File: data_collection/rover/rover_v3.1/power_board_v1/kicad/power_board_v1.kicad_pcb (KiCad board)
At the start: 4 copper layers, 100 x 65 mm, 136 parts, among them J1 XT60_BATT, J10 from Pi USB2, J11 UPDI prog (UPDI/3V3/GND), J12 5V_A pigtail (DNP), J13 USB_A port3 (3A), J14 from Pi USB3, J2 PANEL_SW, J3 USB4105-GF-A (TH shell), J4 USB_A radio1, J5 USB_A radio2, J6 AUX 5V 2A, J7 PI GPIO harness, J8 AUX_CTL out (JST-GH), J9 from Pi USB1, Q2 CSD18543Q3A diode, Q3 CSD18543Q3A switch, U1 LM5145 rail A, U10 TPS2557 ~3A (always on), U2 LM5145 rail B, U3 ATtiny816-SSN (SOIC-20), U4 LM74800-Q1, U5 INA226 (addr 0x40), U6 TPS7A1633 3V3 60V LDO, U7 TPS2557 ~3A, U8 TPS2557 ~3A, U9 AP2112K-3.3 (switched)

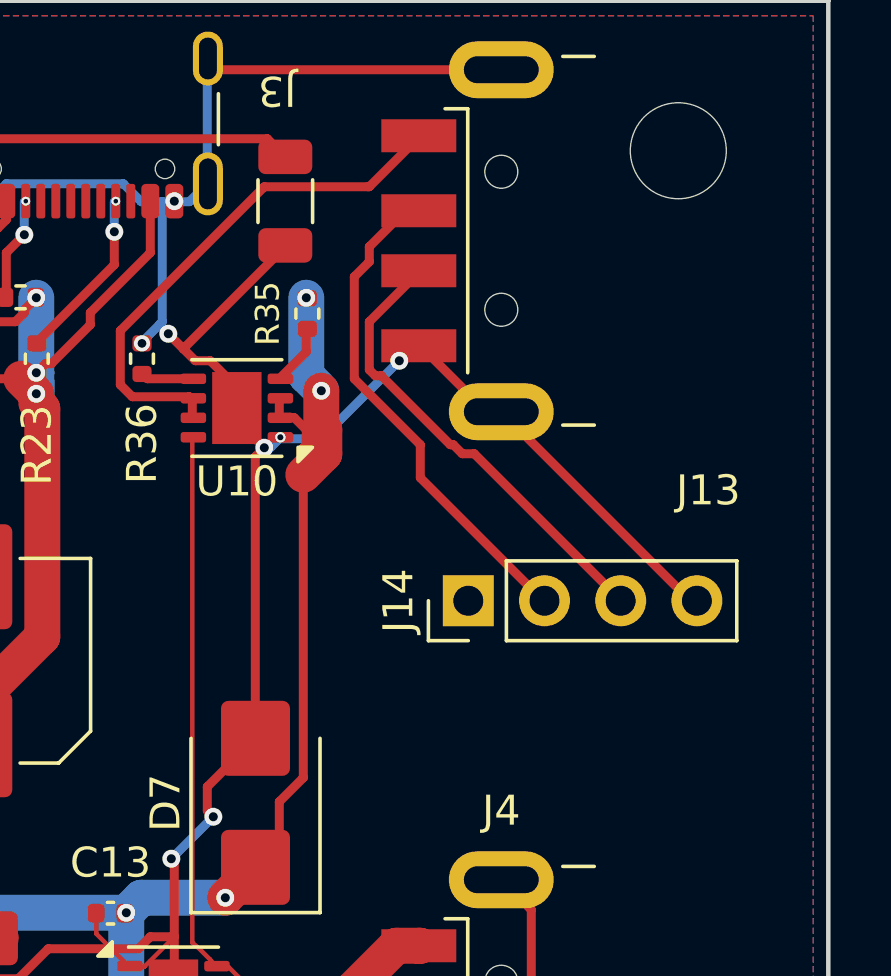
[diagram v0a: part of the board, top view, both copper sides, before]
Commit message: power_board v4.5: add D8 (USB port 3 ESD array) — caught by KiCad 10 schematic-parity
KiCad 10.0.4 re-validation found D8 (USBLC6-2SC6, port 3 ESD) in the
schematic/netlist but absent from the board since v4: the 3-port change
added D8's place() call but not its REF_FP footprint entry, and
generate_board.py silently skipped footprint-less parts. Port 3 data
lines (J14->J13) carried no ESD protection while ports 1/2 had D2/D3.

- board: D8 placed at (138.25,74.16) south of J14; all 6 pads routed
  with exact-collide verification (data stubs F.Cu, VBUS3 via B.Cu lane,
  GND stub+via + pours); one redundant B.Cu GND stitch ripped (pour+plane
  carry GND; DRC 0 unconnected proves it). DRC: 0 violations, 0
  unconnected (severity-all, refill). Audit: PASS (same 3 known warns).
- generators: D8 added to REF_FP; missing footprint is now a HARD ERROR;
  netlist parser whitespace-tolerant (KiCad 10 pretty-prints netlists)
  with parsed-0 guards
- netlist.net regenerated (D8 complete + stale pre-SOIC U3 numbering)
- audit_board.py: KiCad >=9 compat (EDA_UNITS rename; WriteDRCReport
  segfaults headless -> kicad-cli drc fallback)
- fab/: full re-export on KiCad 10 (In1/In2 now .g1/.g2 - v10 protel
  naming; stale v7 gerbers + unused User_* layers removed), BOM line
  USBLC6-2SC6 now D2,D3,D8; upload zip added
- .kicad_pro: KiCad 10 format migration (float cleanup + new keys only;
  all rule floors and severities preserved, .kicad_dru untouched)
- .claude/settings.json: read-only tool allowlist (kicad-cli exports,
  pdftoppm/pdfinfo, rsvg-convert, nvidia-smi queries)
- docs/learnings.md: the silent-skip lesson + parity gate rule

Co-Authored-By: Claude Fable 5 <noreply@anthropic.com>
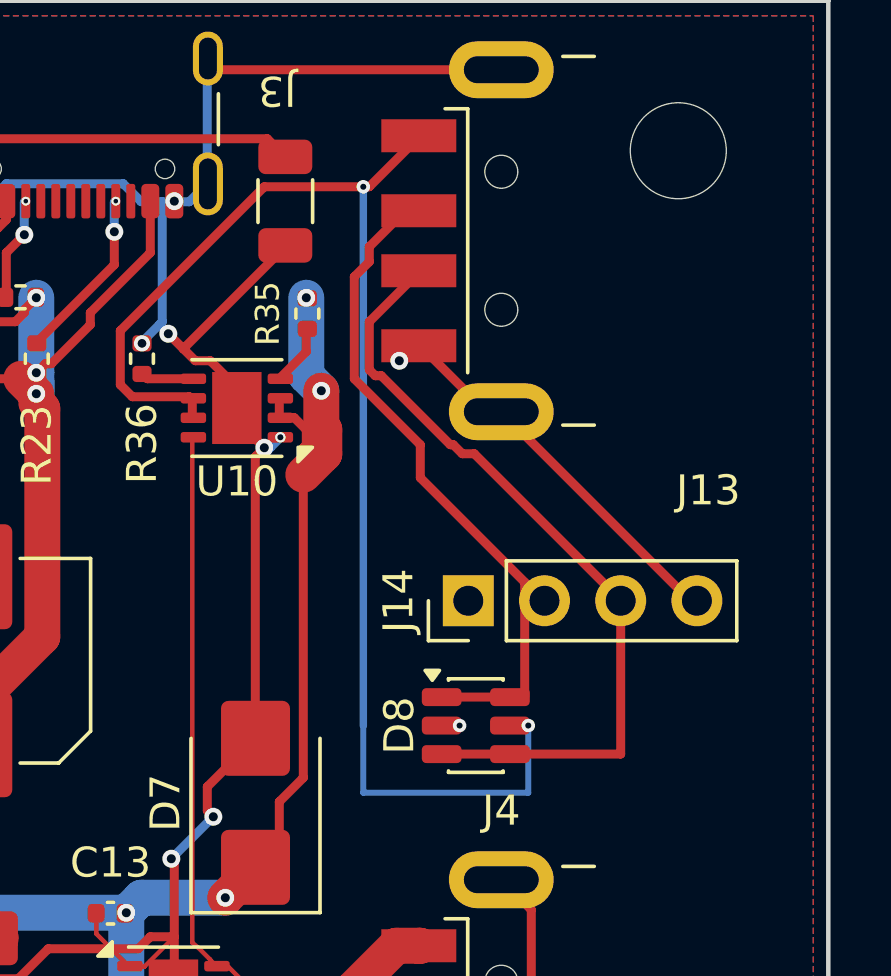
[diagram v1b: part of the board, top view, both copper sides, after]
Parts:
- added D8: USBLC6-2SC6, SOT-23-6, F.Cu at (138.2, 74.2)
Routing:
- net VBUS3: track 17.8 -> 46.4 mm, vias 0 -> 2
- net D3_P: track 15.6 -> 26.7 mm
- net D3_N: track 16.9 -> 23.5 mm
- net GND: track 748.0 -> 743.5 mm, vias 98 -> 99

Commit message: power_board v4.5: sync U3 value to ATtiny1616-SN across generator/sch/netlist/board/BOM/CPL
Closes the drift from the LCSC-only substitution (33571a4): U3's value now
reads 'ATtiny1616-SN (816-compat)' everywhere — schematic PDF, assembly
docs, and BOM Comment agree with the part JLC actually places (C614136).
Also retires the never-orderable 'ATtiny816-SSN' string. DRC/parity
re-verified: 0/0/0. Submission zip rebuilt.

Co-Authored-By: Claude Fable 5 <noreply@anthropic.com>
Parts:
- U3: value ATtiny816-SSN (SOIC-20) -> ATtiny1616-SN (816-compat)
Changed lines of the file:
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@@
 			)
 		)
-		(property "Value" "ATtiny816-SSN (SOIC-20)"
+		(property "Value" "ATtiny1616-SN (816-compat)"
 			(at 0 7.35 0)
 			(layer "F.Fab")

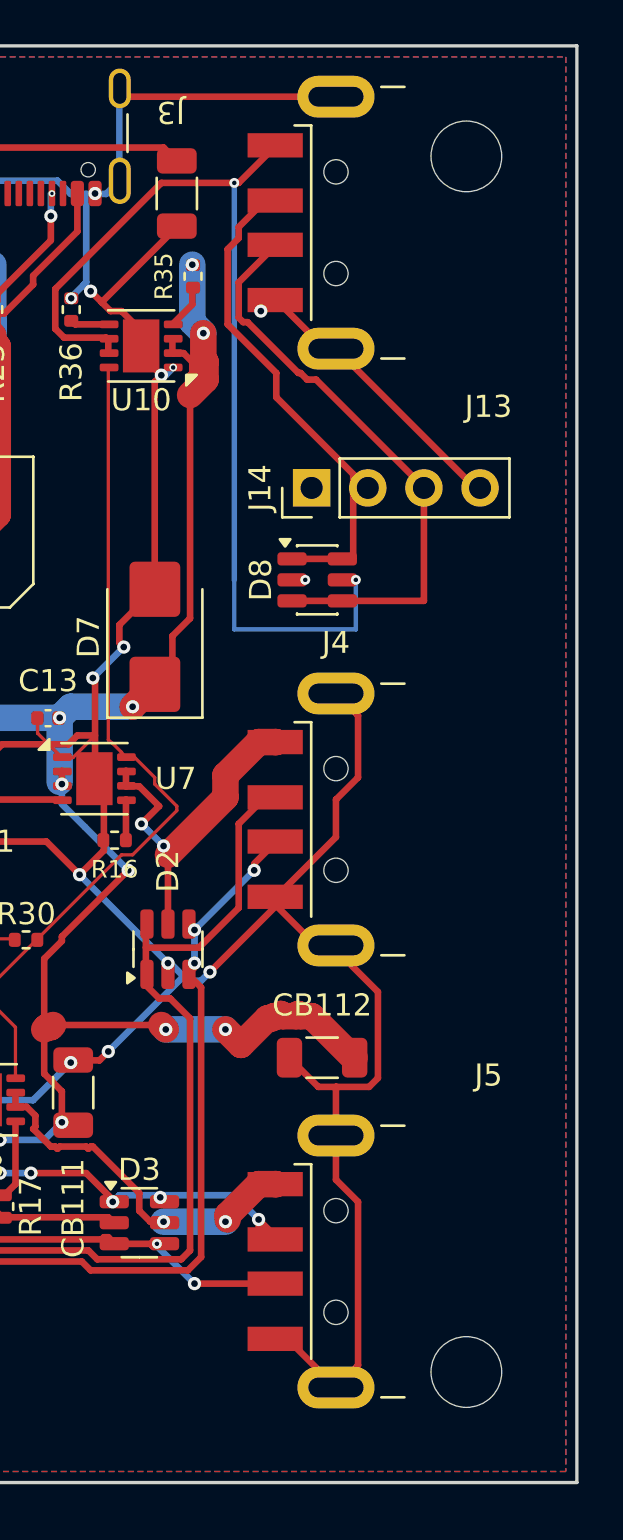
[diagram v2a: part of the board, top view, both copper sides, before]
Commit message: power_board v4.6: relocate H2/H4 mounting holes out from under the USB-A shells
H2 (145,55) and H4 (145,110) sat directly under J13's and J5's metal
shells — no screw access, so only the left-side mounts were usable and
the heavy USB stack was cantilevered. Placement scan (>=2.9mm body
clearance for an M3 head, >=1.9mm copper clearance, all zones checked):

- H2 -> (146.5, 74.75): right edge between J13 and J4, supporting the
  USB stack where insertion force lands. Button/pan-head M3 only (2.9mm
  to J14/J4 bodies — no washer).
- H4 -> (131.5, 110.0): bottom edge inboard of J5 (3.1mm body, 4.2mm
  copper clearance).

Audit I4w body-over-hole warnings cleared (3 warns -> 1); DRC 0/0 with
refill. CHASSIS NOTE: mounting pattern is now an asymmetric quad —
H1(55,55) H3(55,110) H2(146.5,74.75) H4(131.5,110); standoff plate must
match. Fab re-exported, submission zip rebuilt.

Co-Authored-By: Claude Fable 5 <noreply@anthropic.com>
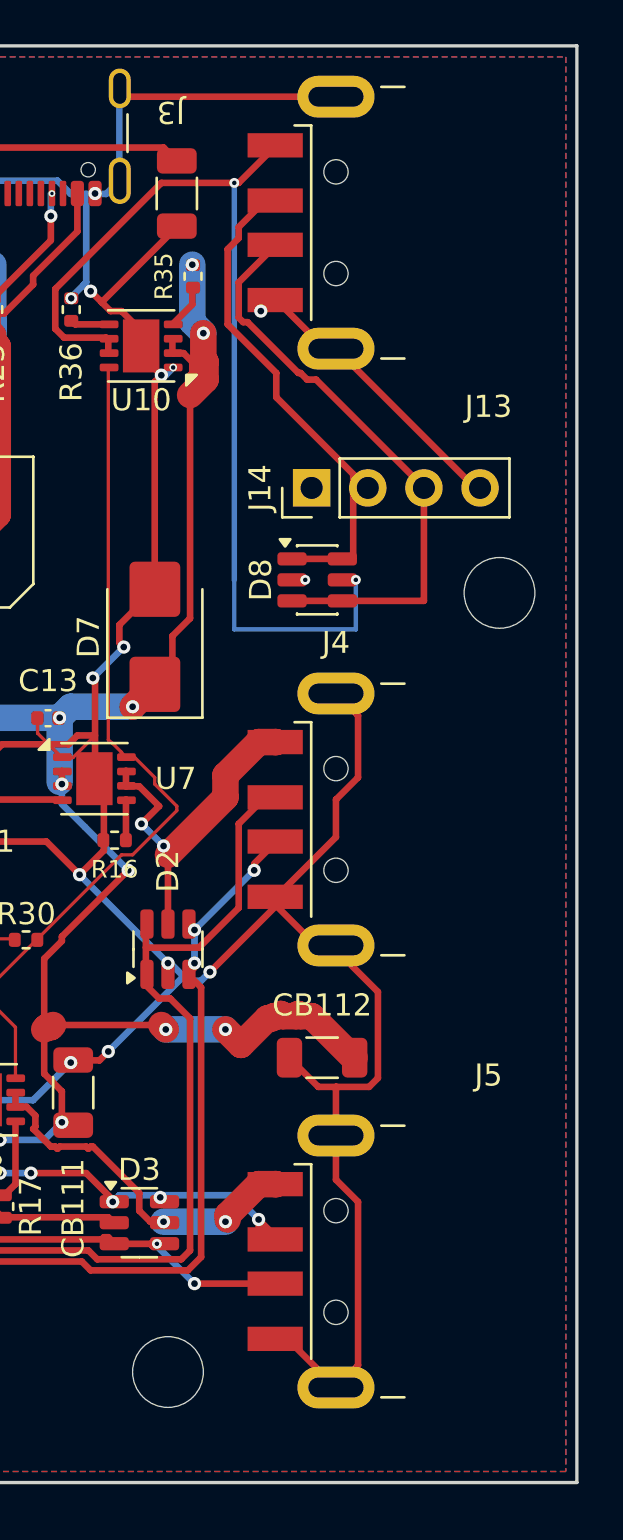
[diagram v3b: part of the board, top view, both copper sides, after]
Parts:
- moved H2 19.8 mm to (146.5, 74.8)
- moved H4 13.5 mm to (131.5, 110.0)
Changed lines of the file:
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@@
 	(footprint "MountingHole_3.2mm_M3"
 		(layer "F.Cu")
-		(at 145 55)
+		(at 146.5 74.75)
 		(descr "Mounting Hole 3.2mm, no annular, M3")
 		(tags "mounting hole 3.2mm no annular m3")
@@
 	(footprint "MountingHole_3.2mm_M3"
 		(layer "F.Cu")
-		(at 145 110)
+		(at 131.5 110)
 		(descr "Mounting Hole 3.2mm, no annular, M3")
 		(tags "mounting hole 3.2mm no annular m3")

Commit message: power_board v4.7: D5 (rev-batt schottky) and D4 (LED) were REVERSED — polarity convention fix
KiCad footprint convention: pad 1 = cathode (verified from the footprints'
own marker graphics). D5 had pin1=VBATT_F -> cathode on the battery side,
blocking the always-on LDO: the supervisor MCU could never power. D4's LED
was reversed. Both invisible to DRC/audit/parity (electrically
self-consistent). Caught during the JLC order polarity audit.

- generator: LED symbol pin1 renamed K, D5/D4 net maps swapped so pin1
  carries the cathode net; structure links updated
- board: D5/D4 rotated 180 with pad nets rebound (copper untouched);
  flipped ref texts relocated
- DRC 0/0, parity clean, audit PASS; fab + submission zip rebuilt
- docs/learnings.md: the bug class and the standing pad1-cathode rule

Co-Authored-By: Claude Fable 5 <noreply@anthropic.com>
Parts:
- turned D4 to 180 degrees
- turned D5 to 0 degrees
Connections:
- D4 pad 1: LED_K -> GND
- D4 pad 2: GND -> LED_K
- D5 pad 1: VBATT_F -> VBATT_FD
- D5 pad 2: VBATT_FD -> VBATT_F
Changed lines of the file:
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@@
 	(footprint "LED_0805_2012Metric"
 		(layer "F.Cu")
-		(at 70.723 104.486)
+		(at 70.723 104.486 180)
 		(descr "LED SMD 0805 (2012 Metric), square (rectangular) end terminal, IPC_7351 nominal, (Body size source: https://docs.google.com/spreadsheets/d/1BsfQQcO9C6DZCsRaXUlFlo91Tg2WpOkGARC1WS5S8t0/edit?usp=sharing), generated with kicad-footprint-generator")
 		(tags "LED")
 		(property "Reference" "D4"
-			(at 0 2.21825 0)
+			(at -0.027 -1.814 0)
 			(layer "F.SilkS")
 			(effects
@@
 		)
 		(property "Value" "green status"
-			(at 0 1.65 0)
+			(at 0 1.65 180)
 			(layer "F.Fab")
 			(effects
@@
 		)
 		(property "Datasheet" ""
-			(at 0 0 0)
+			(at 0 0 180)
 			(layer "F.Fab")
 			(hide yes)
@@
 		)
 		(property "Description" ""
-			(at 0 0 0)
+			(at 0 0 180)
 			(layer "F.Fab")
 			(hide yes)
@@
 		(duplicate_pad_numbers_are_jumpers no)
 		(fp_line
-			(start -1.685 -0.96)
-			(end -1.685 0.96)
+			(start 1 -0.96)
+			(end -1.685 -0.96)
 			(stroke
 				(width 0.12)
@@
 		)
 		(fp_line
-			(start 1 -0.96)
-			(end -1.685 -0.96)
+			(start -1.685 -0.96)
+			(end -1.685 0.96)
 			(stroke
 				(width 0.12)
@@
 		)
 		(fp_line
-			(start -1.68 -0.95)
-			(end 1.68 -0.95)
+			(start 1.68 0.95)
+			(end -1.68 0.95)
 			(stroke
 				(width 0.05)
@@
 		)
 		(fp_line
-			(start -1.68 0.95)
-			(end -1.68 -0.95)
+			(start 1.68 -0.95)
+			(end 1.68 0.95)
 			(stroke
 				(width 0.05)
@@
 		)
 		(fp_line
-			(start 1.68 -0.95)
-			(end 1.68 0.95)
+			(start -1.68 0.95)
+			(end -1.68 -0.95)
 			(stroke
 				(width 0.05)
@@
 		)
 		(fp_line
-			(start 1.68 0.95)
-			(end -1.68 0.95)
+			(start -1.68 -0.95)
+			(end 1.68 -0.95)
 			(stroke
 				(width 0.05)
@@
 		)
 		(fp_line
-			(start -1 -0.3)
-			(end -1 0.6)
+			(start 1 0.6)
+			(end 1 -0.6)
 			(stroke
 				(width 0.1)
@@
 		)
 		(fp_line
-			(start -1 0.6)
-			(end 1 0.6)
+			(start 1 -0.6)
+			(end -0.7 -0.6)
 			(stroke
 				(width 0.1)
@@
 		)
 		(fp_line
-			(start 1 -0.6)
-			(end -0.7 -0.6)
+			(start -1 0.6)
+			(end 1 0.6)
 			(stroke
 				(width 0.1)
@@
 		)
 		(fp_line
-			(start 1 0.6)
-			(end 1 -0.6)
+			(start -1 -0.3)
+			(end -1 0.6)
 			(stroke
 				(width 0.1)
@@
 		)
 		(fp_text user "${REFERENCE}"
-			(at 0 0 0)
+			(at 0 0 180)
 			(layer "F.Fab")
 			(effects
@@
 		)
 		(pad "1" smd roundrect
-			(at -0.9375 0)
+			(at -0.9375 0 180)
 			(size 0.975 1.4)
 			(layers "F.Cu" "F.Mask" "F.Paste")
 			(roundrect_rratio 0.25)
-			(net "LED_K")
+			(net "GND")
 		)
 		(pad "2" smd roundrect
-			(at 0.9375 0)
+			(at 0.9375 0 180)
 			(size 0.975 1.4)
 			(layers "F.Cu" "F.Mask" "F.Paste")
 			(roundrect_rratio 0.25)
-			(net "GND")
+			(net "LED_K")
 		)
 		(embedded_fonts no)
@@
 	(footprint "D_SOD-123"
 		(layer "F.Cu")
-		(at 81.909 75.238 180)
+		(at 81.909 75.238)
 		(descr "SOD-123")
 		(tags "SOD-123")
 		(property "Reference" "D5"
-			(at 0 5.873249 180)
+			(at 0.091 -1.738 0)
 			(layer "F.SilkS")
 			(effects
@@
 		)
 		(property "Value" "B5819W schottky"
-			(at 0 2.1 180)
+			(at 0 2.1 0)
 			(layer "F.Fab")
 			(effects
@@
 		)
 		(property "Datasheet" ""
-			(at 0 0 180)
+			(at 0 0 0)
 			(layer "F.Fab")
 			(hide yes)
@@
 		)
 		(property "Description" ""
-			(at 0 0 180)
+			(at 0 0 0)
 			(layer "F.Fab")
 			(hide yes)
@@
 		(duplicate_pad_numbers_are_jumpers no)
 		(fp_line
-			(start -2.36 1)
-			(end 1.65 1)
+			(start -2.36 -1)
+			(end -2.36 1)
 			(stroke
 				(width 0.12)
@@
 		)
 		(fp_line
-			(start -2.36 -1)
-			(end -2.36 1)
+			(start -2.36 1)
+			(end 1.65 1)
 			(stroke
 				(width 0.12)
@@
 		)
 		(fp_line
-			(start 2.35 1.15)
+			(start -2.35 -1.15)
 			(end -2.35 1.15)
 			(stroke
@@
 		)
 		(fp_line
-			(start 2.35 -1.15)
-			(end 2.35 1.15)
+			(start -2.35 -1.15)
+			(end 2.35 -1.15)
 			(stroke
 				(width 0.05)
@@
 		)
 		(fp_line
-			(start -2.35 -1.15)
-			(end 2.35 -1.15)
+			(start 2.35 -1.15)
+			(end 2.35 1.15)
 			(stroke
 				(width 0.05)
@@
 		)
 		(fp_line
-			(start -2.35 -1.15)
+			(start 2.35 1.15)
 			(end -2.35 1.15)
 			(stroke
@@
 		)
 		(fp_line
-			(start 1.4 0.9)
-			(end -1.4 0.9)
+			(start -1.4 -0.9)
+			(end 1.4 -0.9)
 			(stroke
 				(width 0.1)
@@
 		)
 		(fp_line
-			(start 1.4 -0.9)
-			(end 1.4 0.9)
+			(start -1.4 0.9)
+			(end -1.4 -0.9)
 			(stroke
 				(width 0.1)
@@
 		)
 		(fp_line
-			(start 0.25 0.4)
+			(start -0.75 0)
 			(end -0.35 0)
 			(stroke
@@
 		)
 		(fp_line
-			(start 0.25 0)
-			(end 0.75 0)
+			(start -0.35 0)
+			(end -0.35 -0.55)
 			(stroke
 				(width 0.1)
@@
 		)
 		(fp_line
-			(start 0.25 -0.4)
-			(end 0.25 0.4)
+			(start -0.35 0)
+			(end -0.35 0.55)
 			(stroke
 				(width 0.1)
@@
 		)
 		(fp_line
-			(start -0.35 0)
-			(end -0.35 0.55)
+			(start 0.25 -0.4)
+			(end 0.25 0.4)
 			(stroke
 				(width 0.1)
@@
 		)
 		(fp_line
-			(start -0.35 0)
-			(end -0.35 -0.55)
+			(start 0.25 0)
+			(end 0.75 0)
 			(stroke
 				(width 0.1)
@@
 		)
 		(fp_line
-			(start -0.75 0)
+			(start 0.25 0.4)
 			(end -0.35 0)
 			(stroke
@@
 		)
 		(fp_line
-			(start -1.4 0.9)
-			(end -1.4 -0.9)
+			(start 1.4 -0.9)
+			(end 1.4 0.9)
 			(stroke
 				(width 0.1)
@@
 		)
 		(fp_line
-			(start -1.4 -0.9)
-			(end 1.4 -0.9)
+			(start 1.4 0.9)
+			(end -1.4 0.9)
 			(stroke
 				(width 0.1)
@@
 		)
 		(fp_text user "${REFERENCE}"
-			(at 0 -2 180)
+			(at 0 -2 0)
 			(layer "F.Fab")
 			(effects
@@
 		)
 		(pad "1" smd roundrect
-			(at -1.65 0 180)
+			(at -1.65 0)
 			(size 0.9 1.2)
 			(layers "F.Cu" "F.Mask" "F.Paste")
 			(roundrect_rratio 0.25)
-			(net "VBATT_F")
+			(net "VBATT_FD")
 		)
 		(pad "2" smd roundrect
-			(at 1.65 0 180)
+			(at 1.65 0)
 			(size 0.9 1.2)
 			(layers "F.Cu" "F.Mask" "F.Paste")
 			(roundrect_rratio 0.25)
-			(net "VBATT_FD")
+			(net "VBATT_F")
 		)
 		(embedded_fonts no)

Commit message: power_board v4.8: XT60 battery polarity was REVERSED — + net was on the '-' blade
KiCad's AMASS_XT60PW-M pad 1 is the '-' blade (footprint's own silk +
JLC/EasyEDA data agree). Symbol pin1='+' put VBATT_RAW on it: correctly
wired batteries would present reverse polarity — FE blocks, board DOA.
Third symbol-vs-footprint polarity bug today (after D5/D4).

- symbol pins renamed (1='-', 2='+'), J1 net map swapped, links updated
- board: J1 pad nets swapped; old VBATT_RAW/GND runs ripped; new 1.2mm
  VBATT_RAW run to the north blade -> F1; GND blade via pours/plane
- rotation DB: AMASS_XT60PW-M +270 (board now matches JLC model zero)
- DRC 0/0, parity clean, audit PASS; fab + submission zip rebuilt

Co-Authored-By: Claude Fable 5 <noreply@anthropic.com>
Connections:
- J1 pad 1: VBATT_RAW -> GND
- J1 pad 2: GND -> VBATT_RAW
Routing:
- net GND: track 743.5 -> 735.3 mm
- net VBATT_RAW: track 17.2 -> 15.3 mm
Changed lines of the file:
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@@
 			(remove_unused_layers no)
 			(roundrect_rratio 0.25)
-			(net "VBATT_RAW")
+			(net "GND")
 			(zone_connect 2)
 		)
@@
 			(layers "*.Cu" "*.Mask")
 			(remove_unused_layers no)
-			(net "GND")
+			(net "VBATT_RAW")
 			(zone_connect 2)
 		)
@@
 	)
 	(segment
-		(start 58.8 63)
-		(end 57 64.8)
-		(width 0.3)
-		(layer "F.Cu")
-		(net "GND")
-	)
-	(segment
 		(start 58 100.6)
 		(end 58.9 101.5)
@@
 	)
 	(segment
-		(start 64.5 63)
-		(end 58.8 63)
-		(width 0.3)
-		(layer "F.Cu")
-		(net "GND")
-	)
-	(segment
 		(start 55.3 91.3)
 		(end 55.39 91.25)
@@
 	)
 	(segment
-		(start 61 68)
-		(end 64 68)
+		(start 57.25 64.8)
+		(end 64 64.5)
 		(width 1.2)
 		(layer "F.Cu")
@@
 		(width 1.2)
 		(layer "F.Cu")
-		(net "VBATT_RAW")
-	)
-	(segment
-		(start 57 72)
-		(end 61 68)
-		(width 1.2)
-		(layer "F.Cu")
